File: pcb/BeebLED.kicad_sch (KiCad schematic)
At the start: 14 parts, among them J1 BBC User Port, J2 Jack-DC, J3 WS51282B, U1 74HC14, U2 74LS165

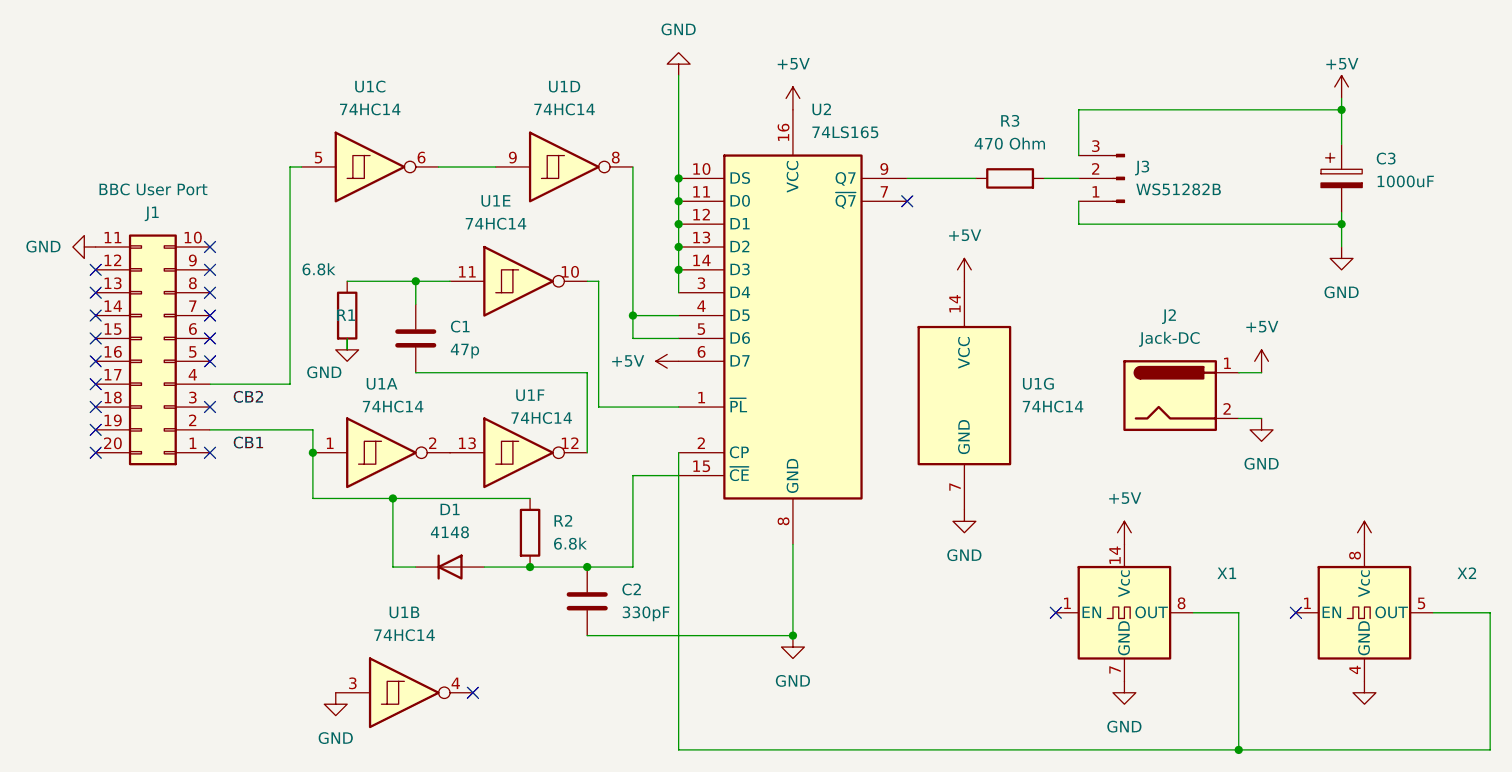
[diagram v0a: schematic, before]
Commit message: Updated to v1.2 schematic and pcb design
Requires further testing
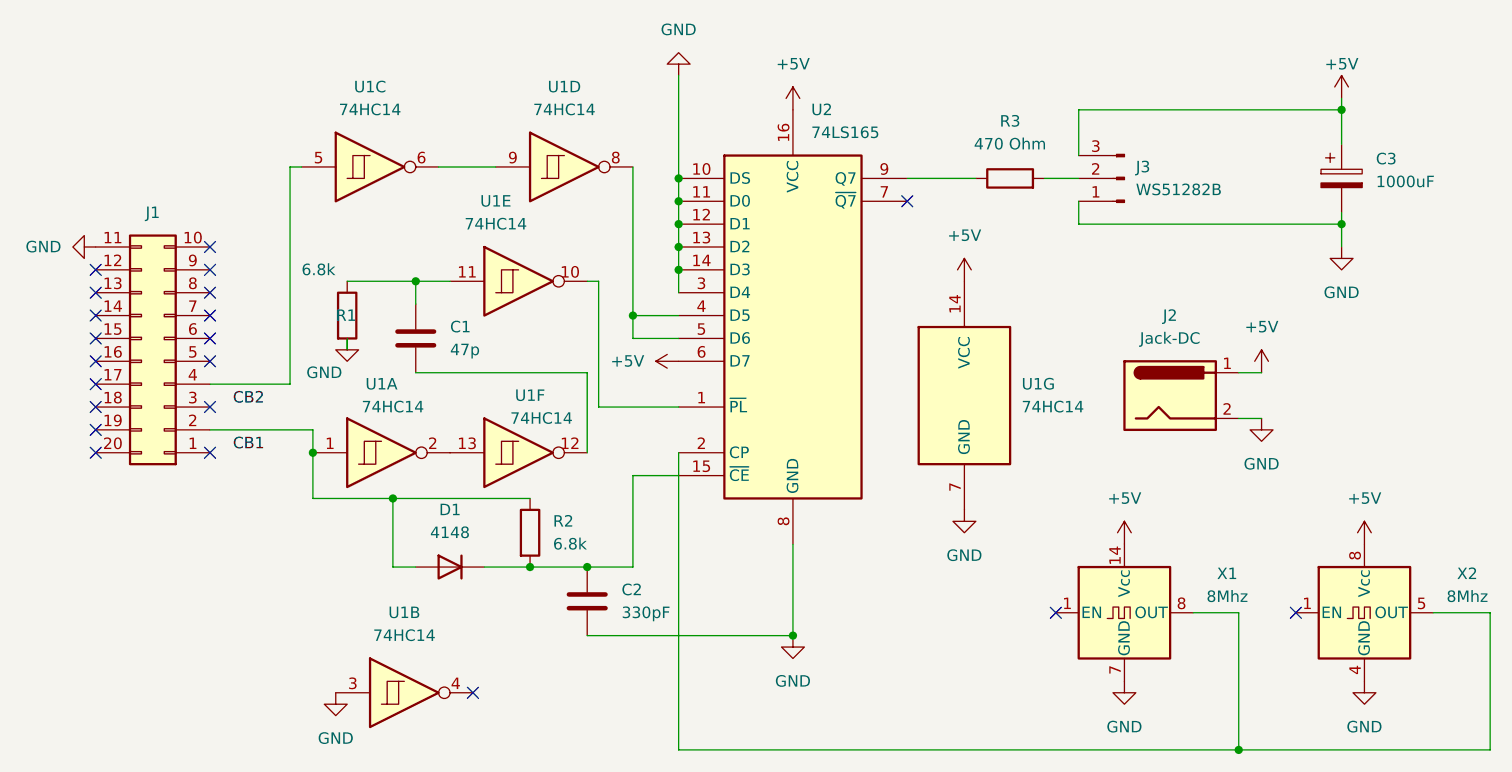
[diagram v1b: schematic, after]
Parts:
- C3: footprint Capacitor_THT:CP_Radial_D5.0mm_P2.50mm -> Capacitor_THT:CP_Radial_D10.0mm_P5.00mm
- J1: value BBC User Port -> (none)
- J3: footprint Connector_JST:JST_PH_S3B-PH-K_1x03_P2.00mm_Horizontal -> Connector_PinHeader_2.54mm:PinHeader_1x03_P2.54mm_Vertical
- X1: value (none) -> 8Mhz; footprint (none) -> Oscillator:Oscillator_DIP-14
- X2: value (none) -> 8Mhz; footprint (none) -> Oscillator:Oscillator_DIP-8
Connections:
- net at J1.2 (Pin_2), R2.1, U1.1: now also D1.1 (A); no longer D1.2 (K)
- net at C2.1, R2.2, U2.15 (~{CE}): now also D1.2 (K); no longer D1.1 (A)
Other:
- moved on the sheet: D1
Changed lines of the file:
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@@
   (title_block
     (title "BeebLed")
-    (date "2023-05-07")
-    (rev "v1.1")
+    (date "2023-05-26")
+    (rev "v1.2")
     (company "!FOZ!")
     (comment 1 "Derived from a design on ABNIELSEN.COM")
@@
     (in_bom yes) (on_board yes)
     (property "Reference" "J1" (id 0) (at 82.55 80.01 0))
-    (property "Value" "BBC User Port" (id 1) (at 82.55 77.47 0))
+    (property "Value" "" (id 1) (at 82.55 77.47 0))
     (property "Footprint" "Connector_IDC:IDC-Header_2x10_P2.54mm_Horizontal" (id 2) (at 83.82 96.52 0)
       (effects (font (size 1.27 1.27)) hide)
@@
     (pin "9")
   )
-  (symbol (lib_id "Simulation_SPICE:DIODE") (at 115.57 119.38 180) (unit 1)
+  (symbol (lib_id "Simulation_SPICE:DIODE") (at 115.57 119.38 0) (mirror x) (unit 1)
     (in_bom yes) (on_board yes) (fields_autoplaced)
     (property "Reference" "D1" (id 0) (at 115.57 113.03 0))
@@
     (in_bom yes) (on_board yes) (fields_autoplaced)
     (property "Reference" "X1" (id 0) (at 201.93 120.1293 0))
-    (property "Value" "" (id 1) (at 201.93 122.6693 0))
-    (property "Footprint" "" (id 2) (at 201.93 133.35 0)
+    (property "Value" "8Mhz" (id 1) (at 201.93 122.6693 0))
+    (property "Footprint" "Oscillator:Oscillator_DIP-14" (id 2) (at 201.93 133.35 0)
       (effects (font (size 1.27 1.27)) hide)
     )
@@
       (effects (font (size 1.27 1.27)) (justify left))
     )
-    (property "Footprint" "Capacitor_THT:CP_Radial_D5.0mm_P2.50mm" (id 2) (at 215.5952 80.01 0)
+    (property "Footprint" "Capacitor_THT:CP_Radial_D10.0mm_P5.00mm" (id 2) (at 215.5952 80.01 0)
       (effects (font (size 1.27 1.27)) hide)
     )
@@
       (effects (font (size 1.27 1.27)) hide)
     )
-    (property "Value" "" (id 1) (at 217.17 137.16 0))
+    (property "Value" "GND" (id 1) (at 217.17 137.16 0))
     (property "Footprint" "" (id 2) (at 217.17 132.08 0)
       (effects (font (size 1.27 1.27)) hide)
@@
       (effects (font (size 1.27 1.27)) hide)
     )
-    (property "Value" "" (id 1) (at 217.17 111.76 0))
+    (property "Value" "+5V" (id 1) (at 217.17 111.76 0))
     (property "Footprint" "" (id 2) (at 217.17 116.84 0)
       (effects (font (size 1.27 1.27)) hide)
@@
     (in_bom yes) (on_board yes) (fields_autoplaced)
     (property "Reference" "X2" (id 0) (at 228.6 120.1293 0))
-    (property "Value" "" (id 1) (at 228.6 122.6693 0))
-    (property "Footprint" "" (id 2) (at 228.6 133.35 0)
+    (property "Value" "8Mhz" (id 1) (at 228.6 122.6693 0))
+    (property "Footprint" "Oscillator:Oscillator_DIP-8" (id 2) (at 228.6 133.35 0)
       (effects (font (size 1.27 1.27)) hide)
     )
@@
       (effects (font (size 1.27 1.27)) (justify right))
     )
-    (property "Footprint" "Connector_JST:JST_PH_S3B-PH-K_1x03_P2.00mm_Horizontal" (id 2) (at 190.5 76.2 0)
+    (property "Footprint" "Connector_PinHeader_2.54mm:PinHeader_1x03_P2.54mm_Vertical" (id 2) (at 190.5 76.2 0)
       (effects (font (size 1.27 1.27)) hide)
     )
@@
     )
     (path "/51121dda-9140-447c-8e6f-b3991e73c49e"
-      (reference "C3") (unit 1) (value "1000uF") (footprint "Capacitor_THT:CP_Radial_D5.0mm_P2.50mm")
+      (reference "C3") (unit 1) (value "1000uF") (footprint "Capacitor_THT:CP_Radial_D10.0mm_P5.00mm")
     )
     (path "/3aaf1361-7b71-452c-aa61-68599d28c9b0"
@@
     )
     (path "/352f2bc0-2898-4caa-a7c1-8fdd76c416aa"
-      (reference "J1") (unit 1) (value "BBC User Port") (footprint "Connector_IDC:IDC-Header_2x10_P2.54mm_Horizontal")
+      (reference "J1") (unit 1) (value "BBC Micro User Port") (footprint "Connector_IDC:IDC-Header_2x10_P2.54mm_Horizontal")
     )
     (path "/5671bdf8-5ef5-4ed5-9232-aa164db62ba9"
@@
     )
     (path "/cbc4f504-99b1-404f-8b3a-f0881c4b1ae5"
-      (reference "J3") (unit 1) (value "WS51282B") (footprint "Connector_JST:JST_PH_S3B-PH-K_1x03_P2.00mm_Horizontal")
+      (reference "J3") (unit 1) (value "WS51282B") (footprint "Connector_PinHeader_2.54mm:PinHeader_1x03_P2.54mm_Vertical")
     )
     (path "/f0c486ea-8fdb-49cc-877f-2ed6f80e037d"
